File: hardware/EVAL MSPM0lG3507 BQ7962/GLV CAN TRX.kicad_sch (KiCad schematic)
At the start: 17 parts, among them U10 MCP2542FDxMF, U5 ISO7721D, U9 LMR51603XDBVR

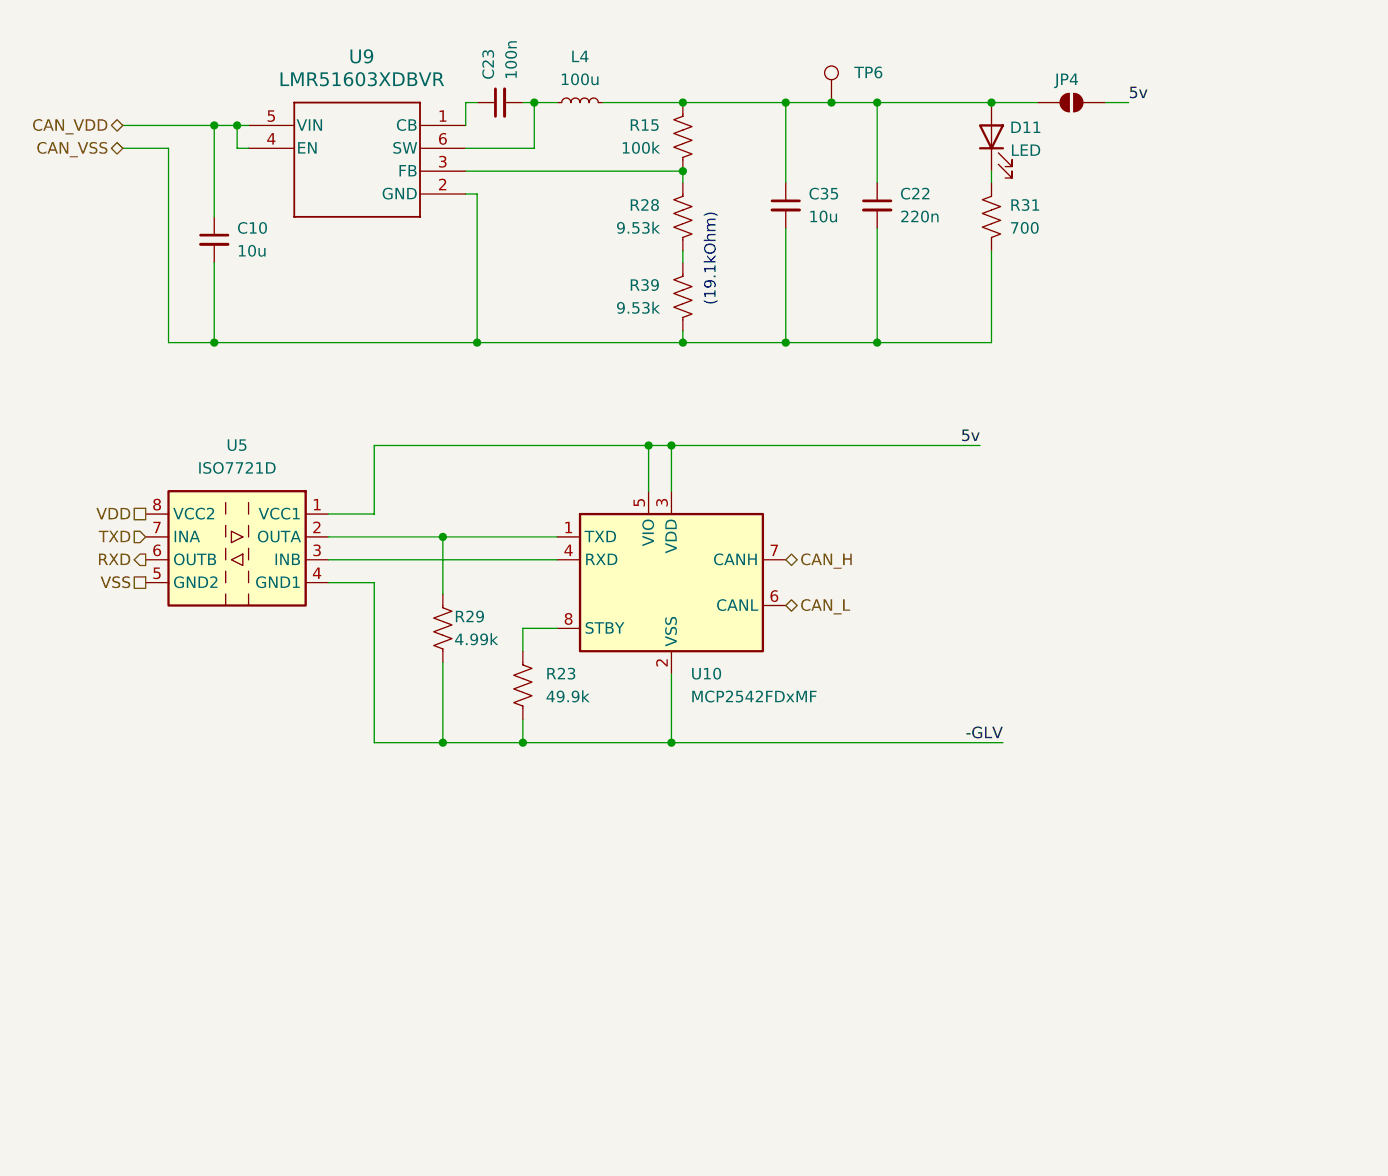
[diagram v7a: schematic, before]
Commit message: indicated layout so someone else can do it
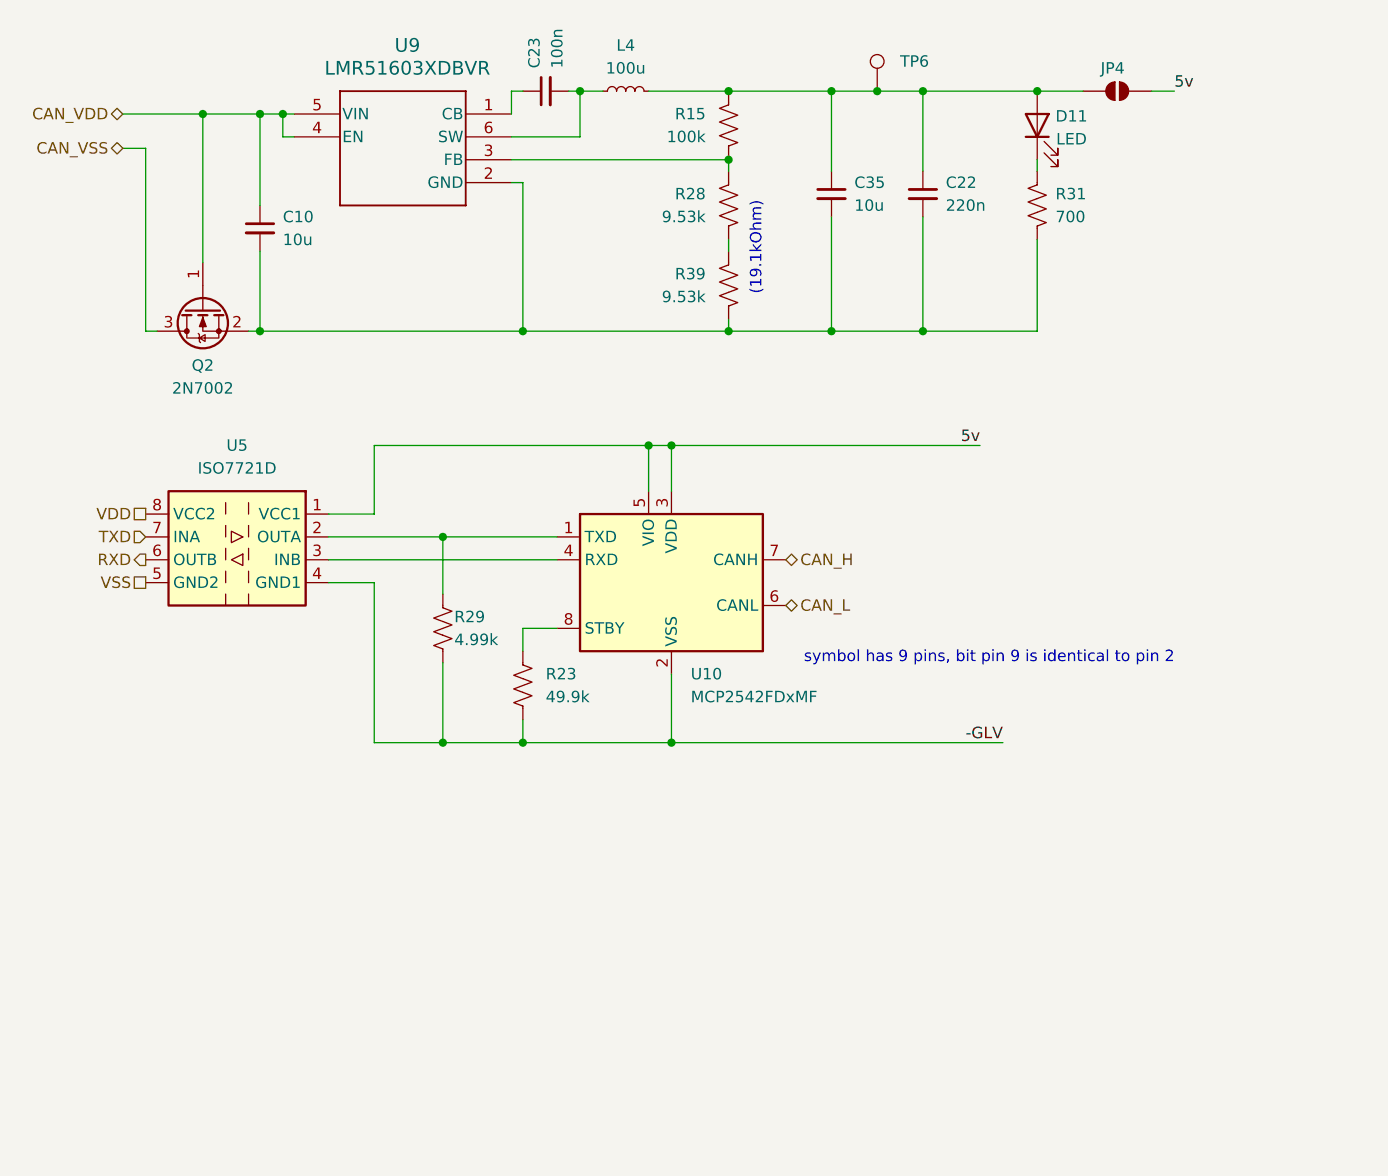
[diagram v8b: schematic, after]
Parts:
- added Q2: 2N7002, Package_TO_SOT_SMD:SOT-23, symbol Transistor_FET:2N7002
- U9: footprint DBV0006A-MFG-IPC_A -> zzLocalLibraries-Footprints:DBV0006A-MFG-IPC_B; mouser (none) -> https://www.mouser.com/ProductDetail/Texas-Instruments/LMR5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; unit x10 (none) -> 0.949
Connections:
- net CAN_VDD: now also Q2.1 (G)
- net CAN_VSS: now also Q2.3 (D); no longer C10.2, C22.2, C35.2, R31.2, R39.1, U9.2 (GND)
- new net: C10.2, C22.2, C35.2, Q2.2 (S), R31.2, R39.1, U9.2 (GND)
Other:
- note added: "symbol has 9 pins, bit pin 9 is identical to pin 2"
- moved on the sheet: C10, C22, C23, C35, D11, JP4, L4, R15, R28, R31, R39, TP6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
